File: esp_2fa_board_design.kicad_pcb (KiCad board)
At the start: 2 copper layers, 82 x 42 mm, 54 parts, among them IC1 TPS22919DCKR, J1 Conn_01x02_Female, J2 TYPE-C-31-M-17, J3 Conn_01x02_Female, Q1 DMP2305U-7, SW5 POWER SWITCH, U1 ESP32-WROOM-32, U2 DS3231M, U3 MCP73831-2-OT, U4 TPS63001

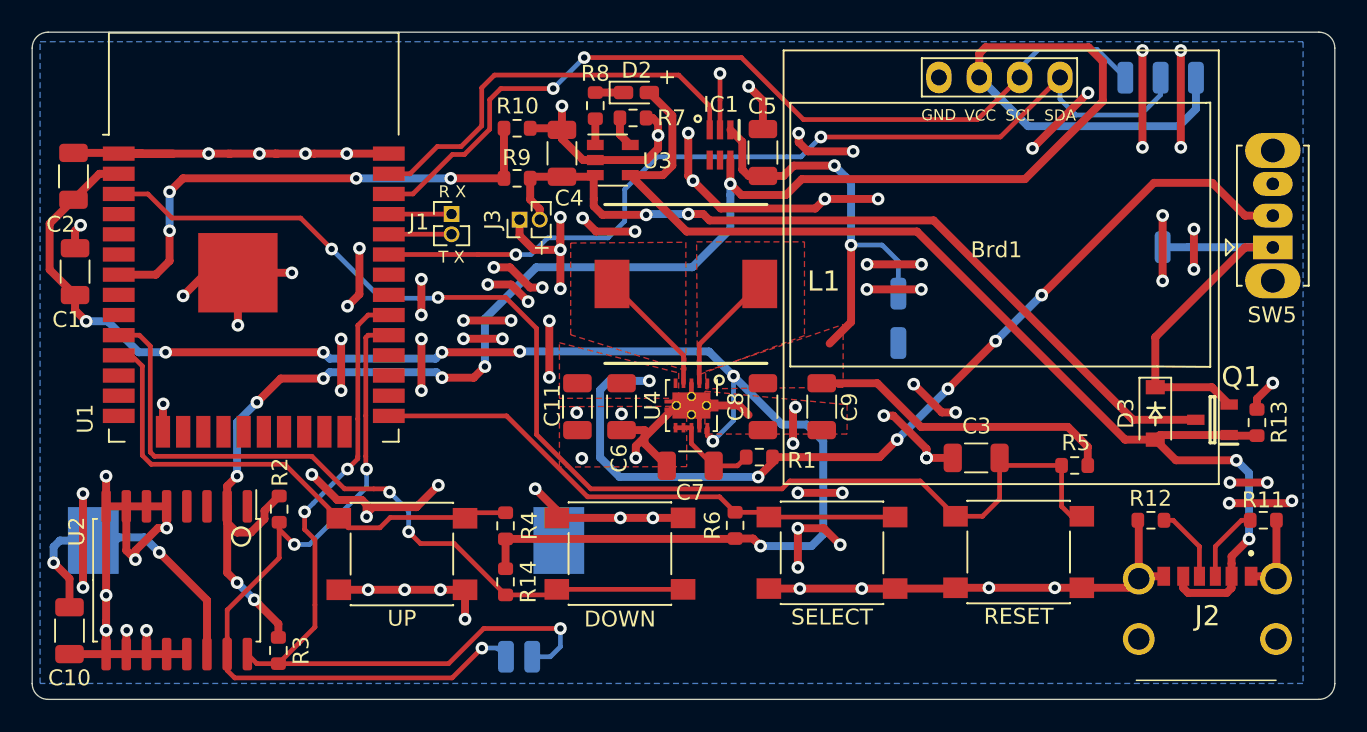
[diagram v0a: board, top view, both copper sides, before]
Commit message: Updated pcb to increase rx/tx header size
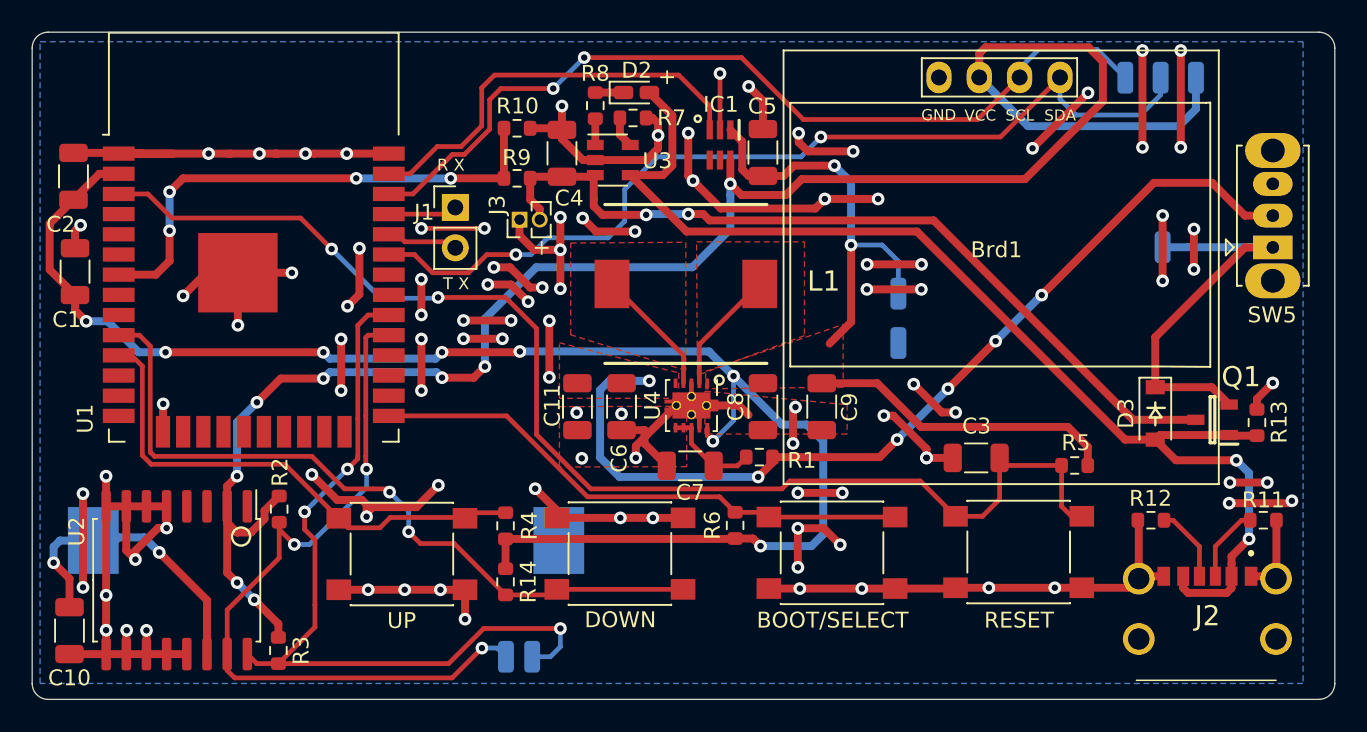
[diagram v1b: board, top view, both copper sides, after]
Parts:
- removed DOWN: DOWN, Button_Switch_SMD:SW_Push_1P1T_NO_6x6mm_H9.5mm
- removed SELECT: BOOT/SELECT, Button_Switch_SMD:SW_Push_1P1T_NO_6x6mm_H9.5mm
- added SW2: DOWN, Button_Switch_SMD:SW_Push_1P1T_NO_6x6mm_H9.5mm, F.Cu at (127.0, 112.8)
- added SW3: BOOT/SELECT, Button_Switch_SMD:SW_Push_1P1T_NO_6x6mm_H9.5mm, F.Cu at (140.3, 112.8)
- J1: footprint Connector_PinHeader_1.27mm:PinHeader_1x02_P1.27mm_Vertical -> Connector_PinHeader_2.54mm:PinHeader_1x02_P2.54mm_Vertical
- moved J1 0.48 mm to (116.6, 91.0)
- renumbered UP to SW1, RESET to SW4
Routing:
- net GND: track 298.1 -> 302.0 mm, vias 101 -> 103
- net /IO21_SDA: track 58.6 -> 59.6 mm
- net /RX: track 3.95 -> 4.55 mm

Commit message: Replaced footprint of switch with custom made
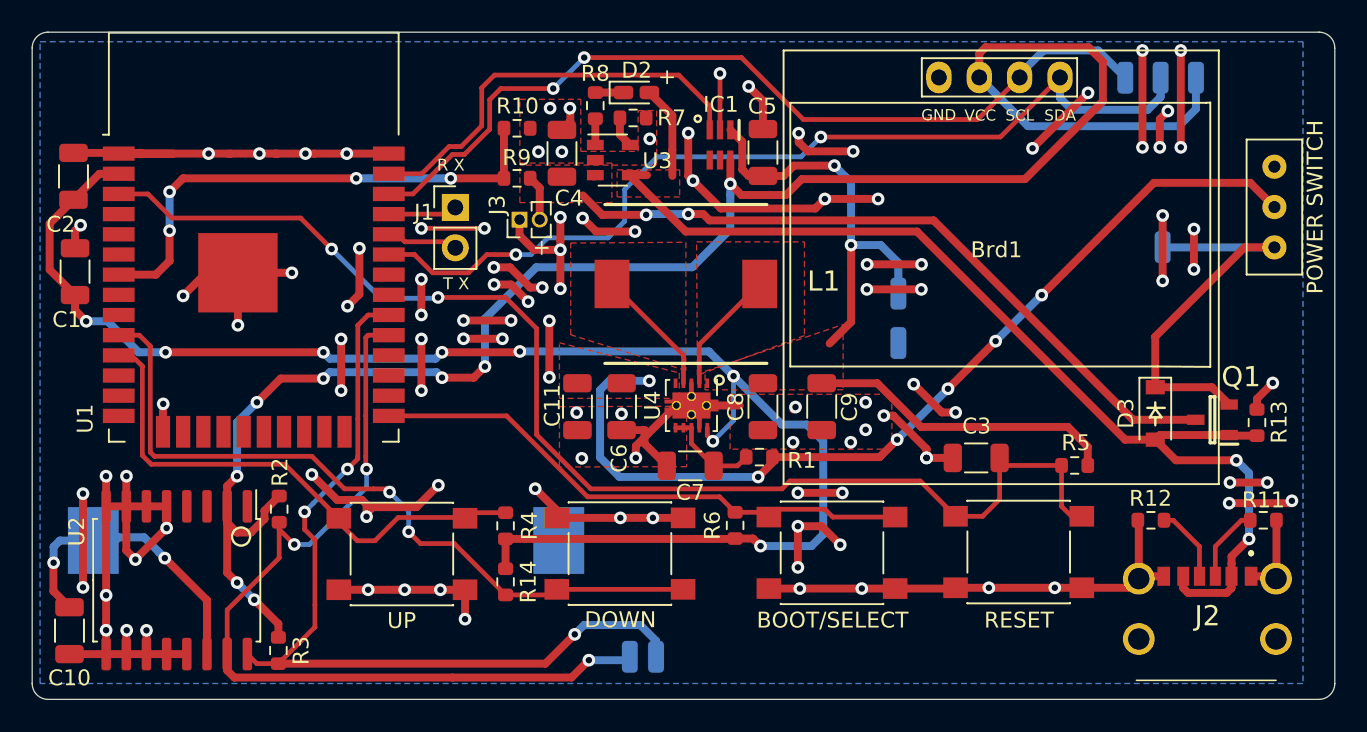
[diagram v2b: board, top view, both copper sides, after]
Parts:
- SW5: footprint Button_Switch_THT:SW_Slide_1P2T_CK_OS102011MS2Q -> slide_switch_12D00:Slide_Switch_SS-12D00
- moved TP3 7.80 mm to (129.3, 119.3)
- moved TP2 7.80 mm to (127.6, 119.3)
- moved SW5 2.54 mm to (168.2, 91.0), turned to 180 degrees
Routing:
- net GND: track 302.0 -> 291.4 mm, vias 103 -> 112
- net /IO5_SDA: track 49.6 -> 56.6 mm
- net +BATT: track 52.5 -> 47.7 mm
- net /IO18_SCL: track 50.2 -> 54.5 mm
- net VBUS: track 73.1 -> 71.9 mm
- net /IO26: track 32.6 -> 33.4 mm
- added copper zone on F.Cu, net +BATT
- added copper zone on F.Cu, net VBUS
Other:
- rule trace_min: 0.000152 -> 0.2
- rule via_min_size: 0.000686 -> 0.4
